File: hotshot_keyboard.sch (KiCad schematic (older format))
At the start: 25 parts, among them SW1 SW_Push, U1 ATmega32U4-MU, Y1 Crystal_GND24_Small

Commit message: pcb progress
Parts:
- removed U1: ATmega32U4-MU, Package_QFP:TQFP-44_10x10mm_P0.8mm, symbol MCU_Microchip_ATmega:ATmega32U4-MU
- added U1: ATmega32U4-AU, Package_QFP:TQFP-44_10x10mm_P0.8mm, symbol MCU_Microchip_ATmega:ATmega32U4-AU
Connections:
- net +5V: now also U1.14 (VCC), U1.2 (UVCC), U1.34 (VCC), U1.7 (VBUS)
- net COL0: now also U1.29 (PB5)
- net COL1: now also U1.28 (PB4)
- net GND: now also U1.5 (UGND)
- net ROW0: now also U1.27 (PD7)
- net ROW1: now also U1.30 (PB6)
- net at R1.1, SW1.2: now also U1.13 (~RESET)
- net at C2.1, Y1.3: now also U1.16 (XTAL2)
- net at C1.1, Y1.1: now also U1.17 (XTAL1)
- net at R3.2: now also U1.3 (D-)
- net at R4.2: now also U1.33 (~HWB~/PE2)
- net at R2.1: now also U1.4 (D+)
- net at C3.1: now also U1.6 (UCAP)
- new net: U1.15 (GND), U1.23 (GND), U1.35 (GND), U1.43 (GND)
- new net: U1.24 (AVCC), U1.44 (AVCC)
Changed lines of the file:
@@
-$EndComp
-$Comp
-L MCU_Microchip_ATmega:ATmega32U4-MU U1
-U 1 1 6047E6B2
-P 5000 3700
-F 0 "U1" H 5000 1811 50  0000 C CNN
-F 1 "ATmega32U4-MU" H 5000 1720 50  0000 C CNN
-F 2 "Package_QFP:TQFP-44_10x10mm_P0.8mm" H 5000 3700 50  0001 C CIN
-F 3 "http://ww1.microchip.com/downloads/en/DeviceDoc/Atmel-7766-8-bit-AVR-ATmega16U4-32U4_Datasheet.pdf" H 5000 3700 50  0001 C CNN
-	1    5000 3700
-	1    0    0    -1
 $EndComp
 $Comp
@@
 $EndComp
 Wire Wire Line
-	5000 5500 4900 5500
-Wire Wire Line
 	4500 5500 4500 5600
-Connection ~ 4900 5500
-Wire Wire Line
-	4900 5500 4500 5500
 $Comp
 L Device:R_Small R2
@@
 Wire Wire Line
 	4900 1900 4900 1750
-Wire Wire Line
-	4900 1900 5000 1900
-Connection ~ 4900 1900
-Connection ~ 5000 1900
-Wire Wire Line
-	5000 1900 5100 1900
 Wire Wire Line
 	4250 2050 4250 2200
@@
 Wire Wire Line
 	6200 4300 6050 4300
+$Comp
+L MCU_Microchip_ATmega:ATmega32U4-AU U1
+U 1 1 6055B00A
+P 5000 3700
+F 0 "U1" H 5000 1811 50  0000 C CNN
+F 1 "ATmega32U4-AU" H 5000 1720 50  0000 C CNN
+F 2 "Package_QFP:TQFP-44_10x10mm_P0.8mm" H 5000 3700 50  0001 C CIN
+F 3 "http://ww1.microchip.com/downloads/en/DeviceDoc/Atmel-7766-8-bit-AVR-ATmega16U4-32U4_Datasheet.pdf" H 5000 3700 50  0001 C CNN
+	1    5000 3700
+	1    0    0    -1
+$EndComp
+Wire Wire Line
+	4900 1900 5000 1900
+Wire Wire Line
+	4500 5500 4900 5500
+Connection ~ 4900 1900
 $EndSCHEMATC

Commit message: update schematics
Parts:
- removed D1, D2, D3, D4: D_Small, Diode_SMD:D_SOD-123, symbol Device:D_Small
- removed MX1, MX2, MX3, MX4: MX-NoLED, MX_Alps_Hybrid:MX-1U, symbol MX_Alps_Hybrid:MX-NoLED
- added F?: 500mA, Fuse:Fuse_1206_3216Metric, symbol Device:Polyfuse_Small
- added J?: AVR-ISP-6, symbol Connector:AVR-ISP-6
- added J?: USB_C_Receptacle_USB2.0, symbol Connector:USB_C_Receptacle_USB2.0
- added R5: 5.1K, Resistor_SMD:R_0805_2012Metric, symbol Device:R_Small
- added R6: 5.1k, Resistor_SMD:R_0805_2012Metric, symbol Device:R_Small
- added U?: PRTR5V0U2X, symbol random-keyboard-parts:PRTR5V0U2X
- C1, C2: value 22pF -> 22p
- C3: value 1uF -> 1u
- C4, C5, C6, C7: value 0.1uF -> 0.1u
- C8: value 10uF -> 10u
- Y1: value Crystal_GND24_Small -> XTAL
- renumbered R4 to R2, R2 to R3, R3 to R4
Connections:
- net +5V: now also U1.24 (AVCC), U1.44 (AVCC), F?.1, J?.2 (VCC)
- net D+: now also R4.1; no longer R3.2
- net D-: now also R3.1; no longer R4.1
- net GND: now also U1.15 (GND), U1.23 (GND), U1.35 (GND), U1.43 (GND), J?.6 (GND), J?.A1 (GND), J?.A12 (GND), J?.B1 (GND), J?.B12 (GND), J?.S1 (SHIELD), R5.2, R6.2, U?.1 (GND)
- net VCC: now also F?.2, J?.A4 (VBUS), J?.A9 (VBUS), J?.B4 (VBUS), J?.B9 (VBUS)
- net at U1.4 (D+): no longer R3.1
- net at R4.2: now also J?.A6 (D+), J?.B6 (D+), U?.2 (IO1); no longer U1.3 (D-)
- net XTAL1: now reaches C1.1, U1.17 (XTAL1), Y1.1
- net XTAL2: now reaches C2.1, U1.16 (XTAL2), Y1.3
- net RESET: now reaches R1.1, SW1.2, U1.13 (~RESET)
- net RESET: now also J?.5 (~RST)
- net MOSI: now reaches U1.10 (PB2)
- net MOSI: now also J?.4 (MOSI)
- net MISO: now reaches U1.11 (PB3)
- net MISO: now also J?.1 (MISO)
- net SCK: now reaches U1.9 (PB1)
- net SCK: now also J?.3 (SCK)
- new net: J?.A7 (D-), J?.B7 (D-), R3.2, U?.3 (IO2)
- new net: J?.A5 (CC1), R5.1
- new net: J?.B5 (CC2), R6.1
- no-connect marks 0 -> 4
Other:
- moved on the sheet: C1, C2, C3, C4, C5, C6, C7, C8, F1, R1, R2, R3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

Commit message: update schematics
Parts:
- removed F1: 500mA, Fuse:Fuse_1206_3216Metric, symbol Device:Polyfuse_Small
- removed USB1: Molex-0548190589, random-keyboard-parts:Molex-0548190589, symbol random-keyboard-parts:Molex-0548190589
- gave numbers to parts that had none: 4
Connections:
- net COL0: now also U1.28 (PB4); no longer U1.29 (PB5)
- net COL1: now also U1.29 (PB5); no longer U1.28 (PB4)
- net D+: now also U1.4 (D+)
- net D-: now also U1.3 (D-)
- net GND: now also R2.2; no longer R2.1
- net ROW0: now also U1.41 (PF0); no longer U1.27 (PD7)
- net ROW1: now also U1.40 (PF1); no longer U1.30 (PB6)
- net VCC: now also U2.4 (VCC)
- net at U1.33 (~HWB~/PE2): now also R2.1; no longer R2.2
- net COL3: now reaches U1.12 (PB7)
- net COL6: now reaches U1.18 (PD0)
- net COL7: now reaches U1.19 (PD1)
- net COL8: now reaches U1.20 (PD2)
- net COL9: now reaches U1.21 (PD3)
- net COL11: now reaches U1.22 (PD5)
- net COL10: now reaches U1.25 (PD4)
- net COL12: now reaches U1.26 (PD6)
- net COL4: now reaches U1.31 (PC6)
- net COL5: now reaches U1.32 (PC7)
- net ROW4: now reaches U1.37 (PF6)
- net ROW3: now reaches U1.38 (PF5)
- net ROW2: now reaches U1.39 (PF4)
- new net COL13: U1.27 (PD7)
- new net COL2: U1.30 (PB6)
- no-connect marks 4 -> 6
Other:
- moved on the sheet: C1, C2, J1, R1, R2, R3, R4, SW1, U1, U2, Y1

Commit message: update pcb
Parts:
- C1, C2, C3, C4, C5, C6, C7, C8: footprint Capacitor_SMD:C_0805_2012Metric -> Capacitor_SMD:C_0805_2012Metric_Pad1.18x1.45mm_HandSolder
- F1: footprint Fuse:Fuse_1206_3216Metric -> Fuse:Fuse_1206_3216Metric_Pad1.42x1.75mm_HandSolder
- J1: footprint (none) -> random-keyboard-parts:Reset_Pretty-Mask
- J2: footprint (none) -> Connector_USB:USB_C_Receptacle_HRO_TYPE-C-31-M-12
- R1, R2, R3, R4, R5, R6: footprint Resistor_SMD:R_0805_2012Metric -> Resistor_SMD:R_0805_2012Metric_Pad1.20x1.40mm_HandSolder
- SW1: footprint random-keyboard-parts:SKQG-1155865 -> Button_Switch_SMD:SW_SPST_SKQG_WithStem
- U2: footprint (none) -> random-keyboard-parts:SOT143B
- Y1: footprint Crystal:Crystal_SMD_3225-4Pin_3.2x2.5mm -> Crystal:Crystal_SMD_3225-4Pin_3.2x2.5mm_HandSoldering
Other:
- moved on the sheet: J1, R3, R4, U2

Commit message: update pcb
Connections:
- net DD-: now reaches J2.A7 (D-), J2.B7 (D-), R3.2, U2.3 (IO2)
- net DD+: now reaches J2.A6 (D+), J2.B6 (D+), R4.2, U2.2 (IO1)
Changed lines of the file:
@@
 Wire Bus Line
 	7900 2850 7900 4850
+Text Label 2000 6300 0    50   ~ 0
+DD-
+Text Label 2000 6400 0    50   ~ 0
+DD+
 $EndSCHEMATC

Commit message: reconfig schematics row/cols
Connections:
- net COL0: now also U1.27 (PD7); no longer U1.28 (PB4)
- net COL1: now also U1.28 (PB4); no longer U1.29 (PB5)
- net COL10: now also U1.8 (PB0); no longer U1.25 (PD4)
- net COL11: now also U1.18 (PD0); no longer U1.22 (PD5)
- net COL12: now also U1.41 (PF0); no longer U1.26 (PD6)
- net COL13: now also U1.19 (PD1); no longer U1.27 (PD7)
- net COL2: now also U1.29 (PB5); no longer U1.30 (PB6)
- net COL3: now also U1.30 (PB6); no longer U1.12 (PB7)
- net COL5: now also U1.26 (PD6); no longer U1.32 (PC7)
- net COL6: now also U1.32 (PC7); no longer U1.18 (PD0)
- net COL7: now also U1.39 (PF4); no longer U1.19 (PD1)
- net COL8: now also U1.40 (PF1); no longer U1.20 (PD2)
- net COL9: now also U1.12 (PB7); no longer U1.21 (PD3)
- net ROW0: now also U1.38 (PF5); no longer U1.41 (PF0)
- net ROW1: now also U1.36 (PF7); no longer U1.40 (PF1)
- net ROW2: now also U1.37 (PF6); no longer U1.39 (PF4)
- net ROW3: now also U1.1 (PE6); no longer U1.38 (PF5)
- net ROW4: now also U1.25 (PD4); no longer U1.37 (PF6)
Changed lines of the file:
@@
 Wire Wire Line
 	6200 6800 6450 6800
+Text Label 7450 4500 2    50   ~ 0
+ROW0
+Text Label 7450 4700 2    50   ~ 0
+ROW1
+Text Label 7450 4600 2    50   ~ 0
+ROW2
+Text Label 7450 4000 2    50   ~ 0
+ROW3
+Text Label 7450 3400 2    50   ~ 0
+ROW4
+Text Label 7450 3700 2    50   ~ 0
+COL0
+Text Label 7450 2200 2    50   ~ 0
+COL1
+Text Label 7450 2300 2    50   ~ 0
+COL2
+Text Label 7450 2800 2    50   ~ 0
+COL6
+Text Label 7450 4400 2    50   ~ 0
+COL7
+Text Label 7450 4300 2    50   ~ 0
+COL8
+Text Label 7450 2500 2    50   ~ 0
+COL9
+Text Label 7450 1800 2    50   ~ 0
+COL10
+Text Label 7450 3000 2    50   ~ 0
+COL11
+Text Label 7450 2400 2    50   ~ 0
+COL3
 Text Label 7450 4200 2    50   ~ 0
-ROW0
-Text Label 7450 4300 2    50   ~ 0
-ROW1
-Text Label 7450 4400 2    50   ~ 0
-ROW2
-Text Label 7450 4500 2    50   ~ 0
-ROW3
-Text Label 7450 4600 2    50   ~ 0
-ROW4
-Text Label 7450 2200 2    50   ~ 0
-COL0
-Text Label 7450 2300 2    50   ~ 0
-COL1
-Text Label 7450 2400 2    50   ~ 0
-COL2
-Text Label 7450 3000 2    50   ~ 0
-COL6
+COL12
 Text Label 7450 3100 2    50   ~ 0
-COL7
-Text Label 7450 3200 2    50   ~ 0
-COL8
-Text Label 7450 3300 2    50   ~ 0
-COL9
-Text Label 7450 3400 2    50   ~ 0
-COL10
-Text Label 7450 3500 2    50   ~ 0
-COL11
-Text Label 7450 2500 2    50   ~ 0
-COL3
-Text Label 7450 3600 2    50   ~ 0
-COL12
-Text Label 7450 3700 2    50   ~ 0
 COL13
 $Sheet
@@
 	7450 3100 7550 3200
 Entry Wire Line
-	7450 3200 7550 3300
-Entry Wire Line
-	7450 3300 7550 3400
-Entry Wire Line
 	7450 3400 7550 3500
 Entry Wire Line
-	7450 3500 7550 3600
-Entry Wire Line
 	7450 3600 7550 3700
 Entry Wire Line
@@
 Wire Wire Line
 	7100 3900 7100 4850
-Text Label 7450 2800 2    50   ~ 0
+Text Label 7450 3600 2    50   ~ 0
 COL5
 Text Label 7450 2700 2    50   ~ 0
@@
 	6600 3600 7450 3600
 Wire Wire Line
-	7450 3500 6600 3500
-Wire Wire Line
 	6600 3400 7450 3400
 Wire Wire Line
-	7450 3300 6600 3300
-Wire Wire Line
-	6600 3200 7450 3200
-Wire Wire Line
 	7450 3100 6600 3100
-Wire Bus Line
-	7550 4850 7900 4850
-NoConn ~ 6600 1800
-NoConn ~ 6600 4000
-NoConn ~ 6600 4700
 Wire Wire Line
 	3700 7050 3850 7050
@@
 	2000 6300 2950 6300
 Connection ~ 2000 6300
-Wire Bus Line
-	7550 2300 7550 4850
-Wire Bus Line
-	7900 2850 7900 4850
 Text Label 2000 6300 0    50   ~ 0
 DD-
 Text Label 2000 6400 0    50   ~ 0
 DD+
+Wire Wire Line
+	6600 4700 7450 4700
+Entry Wire Line
+	7450 4700 7550 4800
+Wire Wire Line
+	6600 4000 7450 4000
+Entry Wire Line
+	7450 4000 7550 4100
+Wire Wire Line
+	6600 1800 7450 1800
+Entry Wire Line
+	7450 1800 7550 1900
+NoConn ~ 6600 3500
+NoConn ~ 6600 3300
+NoConn ~ 6600 3200
+Wire Bus Line
+	7550 4950 7900 4950
+Wire Bus Line
+	7550 1900 7550 4950
+Wire Bus Line
+	7900 2850 7900 4950
 $EndSCHEMATC

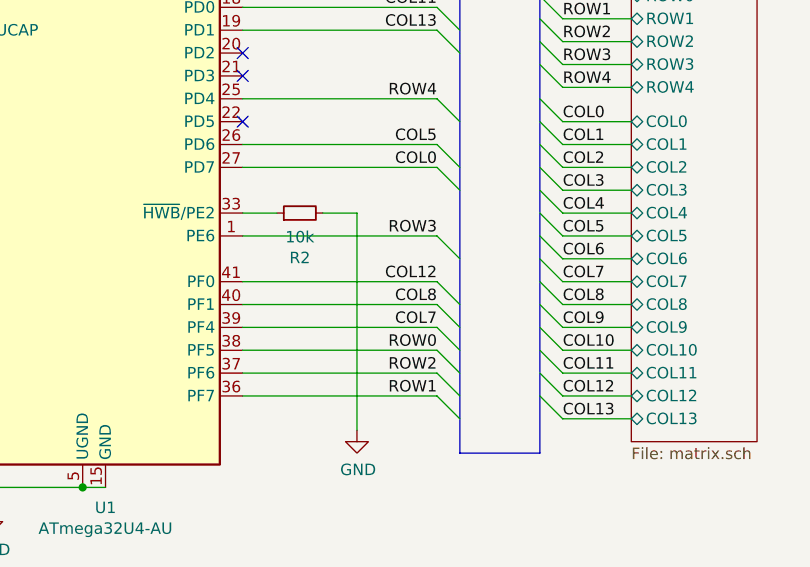
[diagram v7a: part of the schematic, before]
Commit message: update pcb route
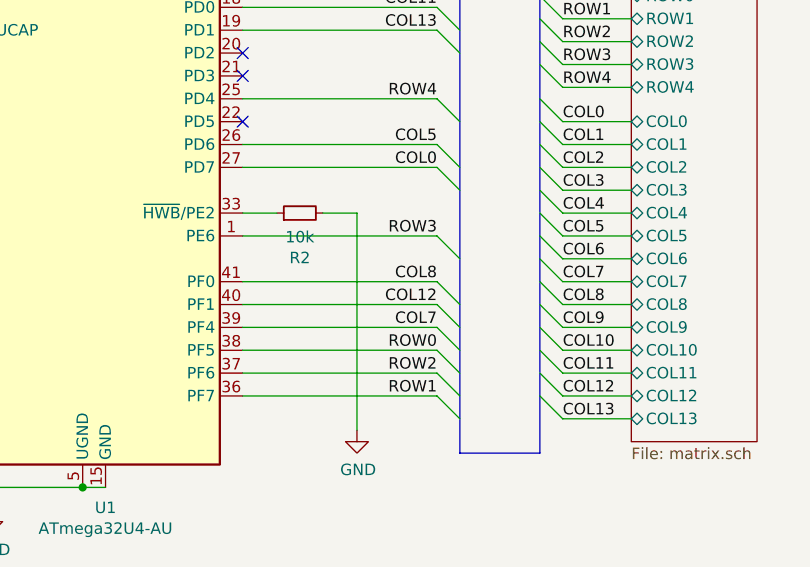
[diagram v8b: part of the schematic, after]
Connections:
- net COL12: now also U1.40 (PF1); no longer U1.41 (PF0)
- net COL8: now also U1.41 (PF0); no longer U1.40 (PF1)
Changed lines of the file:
@@
 Text Label 7450 4400 2    50   ~ 0
 COL7
-Text Label 7450 4300 2    50   ~ 0
+Text Label 7450 4200 2    50   ~ 0
 COL8
 Text Label 7450 2500 2    50   ~ 0
@@
 Text Label 7450 2400 2    50   ~ 0
 COL3
-Text Label 7450 4200 2    50   ~ 0
+Text Label 7450 4300 2    50   ~ 0
 COL12
 Text Label 7450 3100 2    50   ~ 0
